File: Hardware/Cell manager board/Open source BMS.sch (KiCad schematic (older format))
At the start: 53 parts, among them P1 CONN_01X07, P2 EXT-TMP, P3 CONN_01X09, P4 CONN_01X09, Q1 BSS138, Q2 BSS138, Q3 BSS138, Q4 BSS138, Q5 BSS138, Q6 BSS138, U1 ATA6870N_BMS

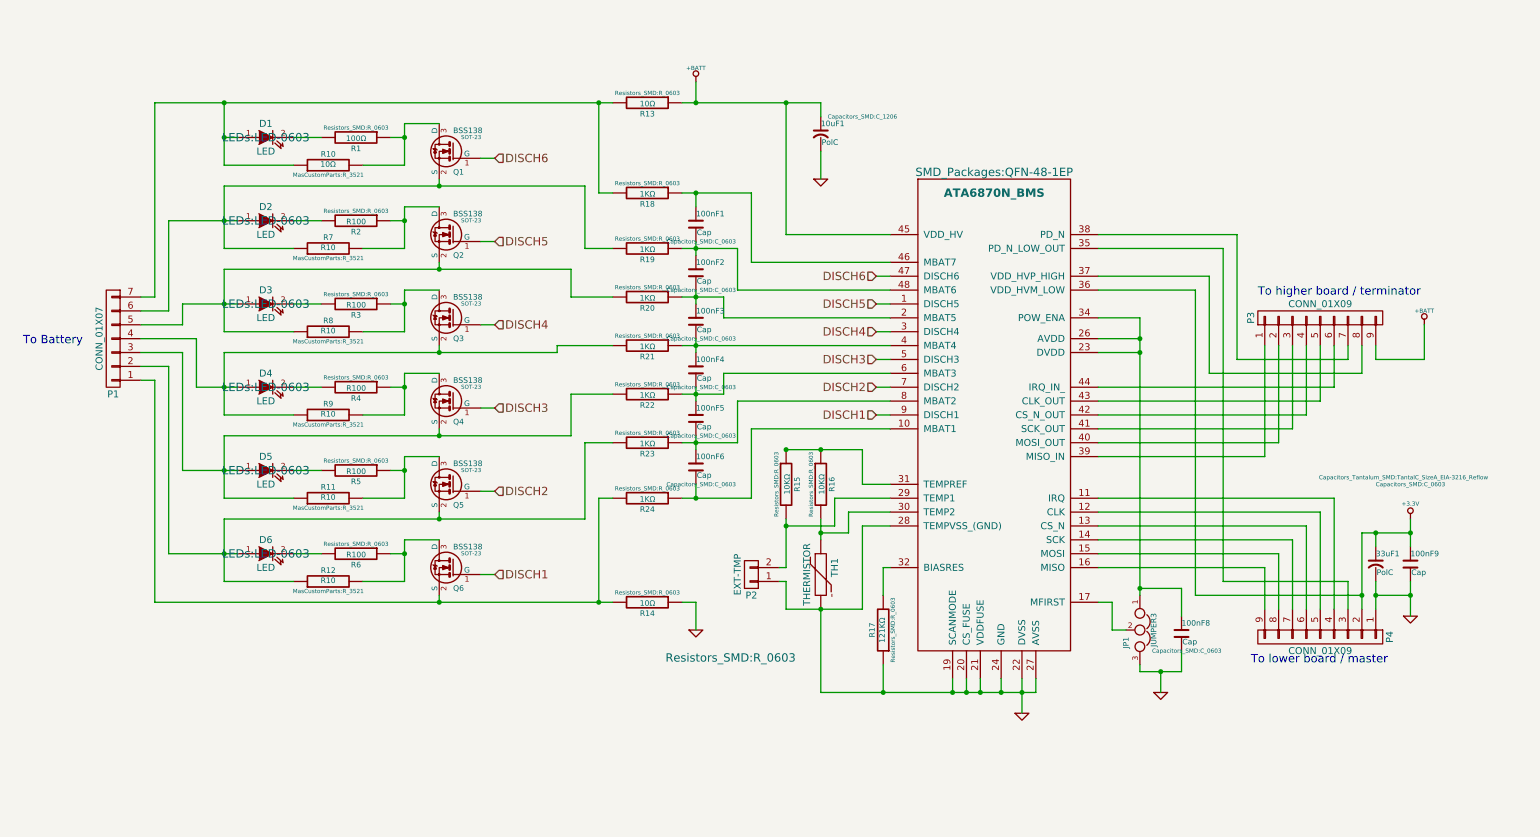
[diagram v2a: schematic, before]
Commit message: cleaned up silkscreen and improved readme
Improved the readme file and added MicroMaster board to it. Also cleaned
up the Slave balance board's silkscreen
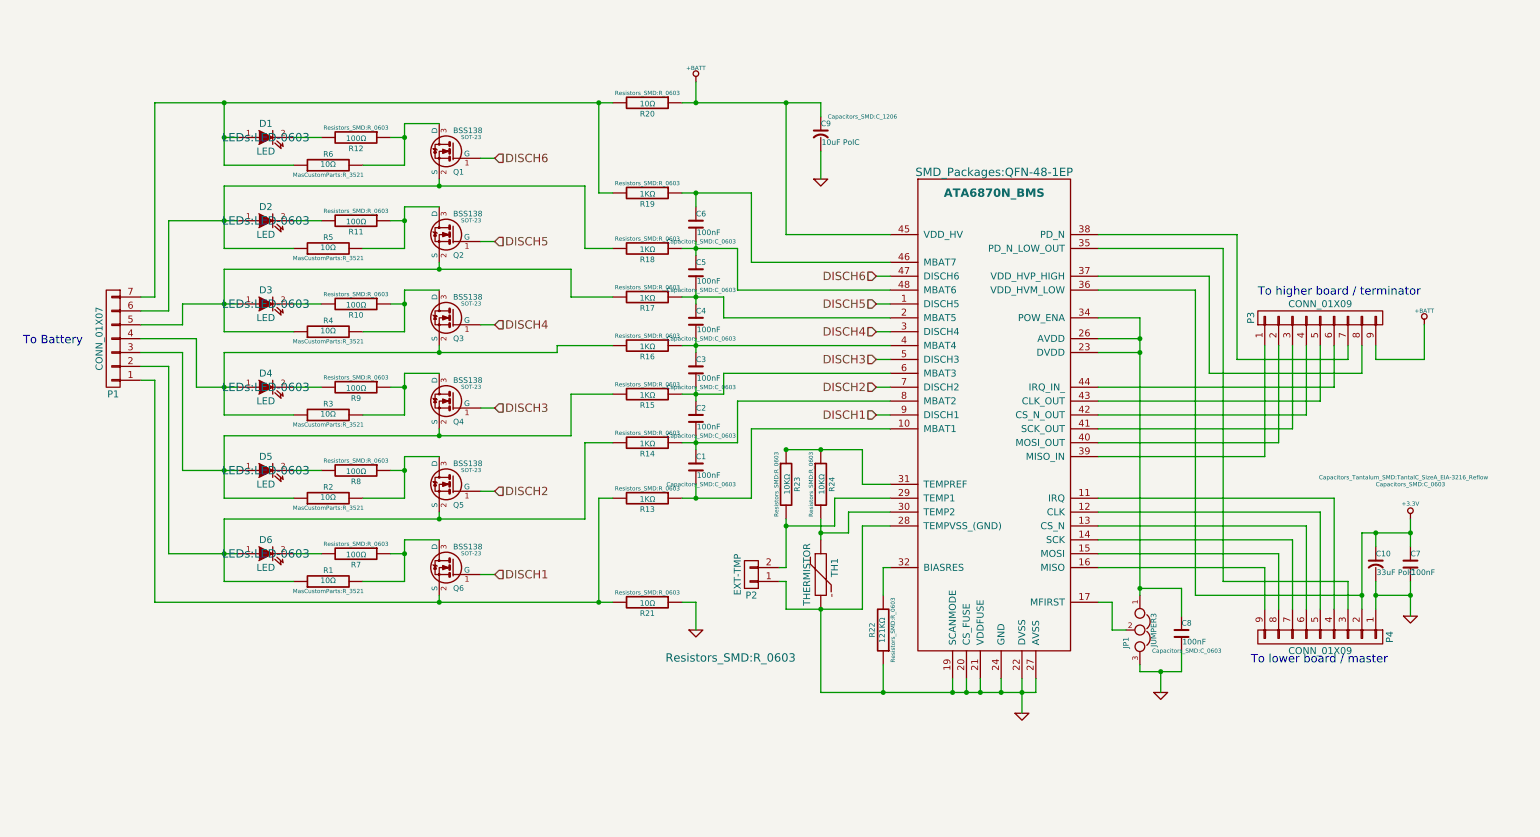
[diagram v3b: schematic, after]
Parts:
- C1: renamed from 100nF6; value Cap -> 100nF
- C10: renamed from 33uF1; value PolC -> 33uF PolC
- C2: renamed from 100nF5; value Cap -> 100nF
- C3: renamed from 100nF4; value Cap -> 100nF
- C4: renamed from 100nF3; value Cap -> 100nF
- C5: renamed from 100nF2; value Cap -> 100nF
- C6: renamed from 100nF1; value Cap -> 100nF
- C7: renamed from 100nF9; value Cap -> 100nF
- C8: renamed from 100nF8; value Cap -> 100nF
- C9: renamed from 10uF1; value PolC -> 10uF PolC
- R1: renamed from R12; value R10 -> 10Ω
- R10: renamed from R3; value R100 -> 100Ω
- R11: renamed from R2; value R100 -> 100Ω
- R2: renamed from R11; value R10 -> 10Ω
- R3: renamed from R9; value R10 -> 10Ω
- R4: renamed from R8; value R10 -> 10Ω
- R5: renamed from R7; value R10 -> 10Ω
- R7: renamed from R6; value R100 -> 100Ω
- R8: renamed from R5; value R100 -> 100Ω
- R9: renamed from R4; value R100 -> 100Ω
- renumbered R1 to R12, R24 to R13, R23 to R14, R22 to R15, R21 to R16, R20 to R17, R19 to R18, R18 to R19, R13 to R20, R14 to R21, R17 to R22, R15 to R23, R16 to R24, R10 to R6
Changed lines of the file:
@@
 $EndComp
 $Comp
-L R R10
+L R R6
 U 1 1 54154E54
 P 2750 1700
-F 0 "R10" V 2830 1700 40  0000 C CNN
+F 0 "R6" V 2830 1700 40  0000 C CNN
 F 1 "10Ω" V 2757 1701 40  0000 C CNN
 F 2 "MasCustomParts:R_3521" V 2680 1700 30  0000 C CNN
@@
 $EndComp
 $Comp
-L R R1
+L R R12
 U 1 1 541899DD
 P 2950 1500
-F 0 "R1" V 3030 1500 40  0000 C CNN
+F 0 "R12" V 3030 1500 40  0000 C CNN
 F 1 "100Ω" V 2957 1501 40  0000 C CNN
 F 2 "Resistors_SMD:R_0603" V 2880 1500 30  0000 C CNN
@@
 $EndComp
 $Comp
-L R R7
+L R R5
 U 1 1 542382CA
 P 2750 2300
-F 0 "R7" V 2830 2300 40  0000 C CNN
-F 1 "R10" V 2757 2301 40  0000 C CNN
+F 0 "R5" V 2830 2300 40  0000 C CNN
+F 1 "10Ω" V 2757 2301 40  0000 C CNN
 F 2 "MasCustomParts:R_3521" V 2680 2300 30  0000 C CNN
 F 3 "" H 2750 2300 30  0000 C CNN
@@
 $EndComp
 $Comp
-L R R2
+L R R11
 U 1 1 542382D0
 P 2950 2100
-F 0 "R2" V 3030 2100 40  0000 C CNN
-F 1 "R100" V 2957 2101 40  0000 C CNN
+F 0 "R11" V 3030 2100 40  0000 C CNN
+F 1 "100Ω" V 2957 2101 40  0000 C CNN
 F 2 "Resistors_SMD:R_0603" V 2880 2100 30  0000 C CNN
 F 3 "" H 2950 2100 30  0000 C CNN
@@
 $EndComp
 $Comp
-L R R8
+L R R4
 U 1 1 5423878A
 P 2750 2900
-F 0 "R8" V 2830 2900 40  0000 C CNN
-F 1 "R10" V 2757 2901 40  0000 C CNN
+F 0 "R4" V 2830 2900 40  0000 C CNN
+F 1 "10Ω" V 2757 2901 40  0000 C CNN
 F 2 "MasCustomParts:R_3521" V 2680 2900 30  0000 C CNN
 F 3 "" H 2750 2900 30  0000 C CNN
@@
 $EndComp
 $Comp
-L R R3
+L R R10
 U 1 1 54238790
 P 2950 2700
-F 0 "R3" V 3030 2700 40  0000 C CNN
-F 1 "R100" V 2957 2701 40  0000 C CNN
+F 0 "R10" V 3030 2700 40  0000 C CNN
+F 1 "100Ω" V 2957 2701 40  0000 C CNN
 F 2 "Resistors_SMD:R_0603" V 2880 2700 30  0000 C CNN
 F 3 "" H 2950 2700 30  0000 C CNN
@@
 $EndComp
 $Comp
-L R R12
+L R R1
 U 1 1 54238D83
 P 2750 4700
-F 0 "R12" V 2830 4700 40  0000 C CNN
-F 1 "R10" V 2757 4701 40  0000 C CNN
+F 0 "R1" V 2830 4700 40  0000 C CNN
+F 1 "10Ω" V 2757 4701 40  0000 C CNN
 F 2 "MasCustomParts:R_3521" V 2680 4700 30  0000 C CNN
 F 3 "" H 2750 4700 30  0000 C CNN
@@
 $EndComp
 $Comp
-L R R6
+L R R7
 U 1 1 54238D89
 P 2950 4500
-F 0 "R6" V 3030 4500 40  0000 C CNN
-F 1 "R100" V 2957 4501 40  0000 C CNN
+F 0 "R7" V 3030 4500 40  0000 C CNN
+F 1 "100Ω" V 2957 4501 40  0000 C CNN
 F 2 "Resistors_SMD:R_0603" V 2880 4500 30  0000 C CNN
 F 3 "" H 2950 4500 30  0000 C CNN
@@
 $EndComp
 $Comp
-L R R9
+L R R3
 U 1 1 54239053
 P 2750 3500
-F 0 "R9" V 2830 3500 40  0000 C CNN
-F 1 "R10" V 2757 3501 40  0000 C CNN
+F 0 "R3" V 2830 3500 40  0000 C CNN
+F 1 "10Ω" V 2757 3501 40  0000 C CNN
 F 2 "MasCustomParts:R_3521" V 2680 3500 30  0000 C CNN
 F 3 "" H 2750 3500 30  0000 C CNN
@@
 $EndComp
 $Comp
-L R R4
+L R R9
 U 1 1 54239059
 P 2950 3300
-F 0 "R4" V 3030 3300 40  0000 C CNN
-F 1 "R100" V 2957 3301 40  0000 C CNN
+F 0 "R9" V 3030 3300 40  0000 C CNN
+F 1 "100Ω" V 2957 3301 40  0000 C CNN
 F 2 "Resistors_SMD:R_0603" V 2880 3300 30  0000 C CNN
 F 3 "" H 2950 3300 30  0000 C CNN
@@
 $EndComp
 $Comp
-L R R11
+L R R2
 U 1 1 542395DF
 P 2750 4100
-F 0 "R11" V 2830 4100 40  0000 C CNN
-F 1 "R10" V 2757 4101 40  0000 C CNN
+F 0 "R2" V 2830 4100 40  0000 C CNN
+F 1 "10Ω" V 2757 4101 40  0000 C CNN
 F 2 "MasCustomParts:R_3521" V 2680 4100 30  0000 C CNN
 F 3 "" H 2750 4100 30  0000 C CNN
@@
 $EndComp
 $Comp
-L R R5
+L R R8
 U 1 1 542395E5
 P 2950 3900
-F 0 "R5" V 3030 3900 40  0000 C CNN
-F 1 "R100" V 2957 3901 40  0000 C CNN
+F 0 "R8" V 3030 3900 40  0000 C CNN
+F 1 "100Ω" V 2957 3901 40  0000 C CNN
 F 2 "Resistors_SMD:R_0603" V 2880 3900 30  0000 C CNN
 F 3 "" H 2950 3900 30  0000 C CNN
@@
 $EndComp
 $Comp
-L R R13
+L R R20
 U 1 1 54244F8C
 P 5050 1250
-F 0 "R13" V 5130 1250 40  0000 C CNN
+F 0 "R20" V 5130 1250 40  0000 C CNN
 F 1 "10Ω" V 5057 1251 40  0000 C CNN
 F 2 "Resistors_SMD:R_0603" V 4980 1250 30  0000 C CNN
@@
 $EndComp
 $Comp
-L R R17
+L R R22
 U 1 1 5424DD8C
 P 6750 5050
-F 0 "R17" V 6830 5050 40  0000 C CNN
+F 0 "R22" V 6830 5050 40  0000 C CNN
 F 1 "121KΩ" V 6757 5051 40  0000 C CNN
 F 2 "Resistors_SMD:R_0603" V 6680 5050 30  0000 C CNN
@@
 $EndComp
 $Comp
-L Cap 100nF2
+L Cap C5
 U 1 1 54250229
 P 5400 2500
-F 0 "100nF2" H 5400 2600 40  0000 L CNN
-F 1 "Cap" H 5406 2465 40  0000 L CNN
+F 0 "C5" H 5400 2600 40  0000 L CNN
+F 1 "100nF" H 5406 2465 40  0000 L CNN
 F 2 "Capacitors_SMD:C_0603" H 5438 2400 30  0000 C CNN
 F 3 "" H 5250 2500 60  0000 C CNN
@@
 $EndComp
 $Comp
-L Cap 100nF4
+L Cap C3
 U 1 1 5425373F
 P 5400 3200
-F 0 "100nF4" H 5400 3300 40  0000 L CNN
-F 1 "Cap" H 5406 3165 40  0000 L CNN
+F 0 "C3" H 5400 3300 40  0000 L CNN
+F 1 "100nF" H 5406 3165 40  0000 L CNN
 F 2 "Capacitors_SMD:C_0603" H 5438 3100 30  0000 C CNN
 F 3 "" H 5250 3200 60  0000 C CNN
@@
 $EndComp
 $Comp
-L Cap 100nF5
+L Cap C2
 U 1 1 54253CD6
 P 5400 3550
-F 0 "100nF5" H 5400 3650 40  0000 L CNN
-F 1 "Cap" H 5406 3515 40  0000 L CNN
+F 0 "C2" H 5400 3650 40  0000 L CNN
+F 1 "100nF" H 5406 3515 40  0000 L CNN
 F 2 "Capacitors_SMD:C_0603" H 5438 3450 30  0000 C CNN
 F 3 "" H 5250 3550 60  0000 C CNN
@@
 $EndComp
 $Comp
-L Cap 100nF6
+L Cap C1
 U 1 1 54253FA8
 P 5400 3900
-F 0 "100nF6" H 5400 4000 40  0000 L CNN
-F 1 "Cap" H 5406 3865 40  0000 L CNN
+F 0 "C1" H 5400 4000 40  0000 L CNN
+F 1 "100nF" H 5406 3865 40  0000 L CNN
 F 2 "Capacitors_SMD:C_0603" H 5438 3800 30  0000 C CNN
 F 3 "" H 5250 3900 60  0000 C CNN
@@
 $EndComp
 $Comp
-L Cap 100nF3
+L Cap C4
 U 1 1 5425B775
 P 5400 2850
-F 0 "100nF3" H 5400 2950 40  0000 L CNN
-F 1 "Cap" H 5406 2815 40  0000 L CNN
+F 0 "C4" H 5400 2950 40  0000 L CNN
+F 1 "100nF" H 5406 2815 40  0000 L CNN
 F 2 "Capacitors_SMD:C_0603" H 5438 2750 30  0000 C CNN
 F 3 "" H 5250 2850 60  0000 C CNN
@@
 $EndComp
 $Comp
-L R R15
+L R R23
 U 1 1 542607A6
 P 6050 4000
-F 0 "R15" V 6130 4000 40  0000 C CNN
+F 0 "R23" V 6130 4000 40  0000 C CNN
 F 1 "10KΩ" V 6057 4001 40  0000 C CNN
 F 2 "Resistors_SMD:R_0603" V 5980 4000 30  0000 C CNN
@@
 $EndComp
 $Comp
-L R R16
+L R R24
 U 1 1 5426080C
 P 6300 4000
-F 0 "R16" V 6380 4000 40  0000 C CNN
+F 0 "R24" V 6380 4000 40  0000 C CNN
 F 1 "10KΩ" V 6307 4001 40  0000 C CNN
 F 2 "Resistors_SMD:R_0603" V 6230 4000 30  0000 C CNN
@@
 $EndComp
 $Comp
-L PolC 33uF1
+L PolC C10
 U 1 1 5426A451
 P 10300 4600
-F 0 "33uF1" H 10300 4700 40  0000 L CNN
-F 1 "PolC" H 10306 4565 40  0000 L CNN
+F 0 "C10" H 10300 4700 40  0000 L CNN
+F 1 "33uF PolC" H 10306 4565 40  0000 L CNN
 F 2 "Capacitors_Tantalum_SMD:TantalC_SizeA_EIA-3216_Reflow" H 10500 5250 30  0000 C CNN
 F 3 "" H 10150 4600 60  0000 C CNN
@@
 $EndComp
 $Comp
-L Cap 100nF9
+L Cap C7
 U 1 1 5425B34F
 P 10550 4600
-F 0 "100nF9" H 10550 4700 40  0000 L CNN
-F 1 "Cap" H 10556 4565 40  0000 L CNN
+F 0 "C7" H 10550 4700 40  0000 L CNN
+F 1 "100nF" H 10556 4565 40  0000 L CNN
 F 2 "Capacitors_SMD:C_0603" H 10550 5200 30  0000 C CNN
 F 3 "" H 10400 4600 60  0000 C CNN
@@
 $EndComp
 $Comp
-L PolC 10uF1
+L PolC C9
 U 1 1 5425B3F6
 P 6300 1500
-F 0 "10uF1" H 6300 1600 40  0000 L CNN
-F 1 "PolC" H 6306 1465 40  0000 L CNN
+F 0 "C9" H 6300 1600 40  0000 L CNN
+F 1 "10uF PolC" H 6306 1465 40  0000 L CNN
 F 2 "Capacitors_SMD:C_1206" H 6600 1650 30  0000 C CNN
 F 3 "" H 6150 1500 60  0000 C CNN
@@
 $EndComp
 $Comp
-L Cap 100nF8
+L Cap C8
 U 1 1 5425D822
 P 8900 5100
-F 0 "100nF8" H 8900 5200 40  0000 L CNN
-F 1 "Cap" H 8906 5065 40  0000 L CNN
+F 0 "C8" H 8900 5200 40  0000 L CNN
+F 1 "100nF" H 8906 5065 40  0000 L CNN
 F 2 "Capacitors_SMD:C_0603" H 8938 5000 30  0000 C CNN
 F 3 "" H 8750 5100 60  0000 C CNN
@@
 Connection ~ 6300 4900
 $Comp
-L R R14
+L R R21
 U 1 1 5426CD58
 P 5050 4850
-F 0 "R14" V 5130 4850 40  0000 C CNN
+F 0 "R21" V 5130 4850 40  0000 C CNN
 F 1 "10Ω" V 5057 4851 40  0000 C CNN
 F 2 "Resistors_SMD:R_0603" V 4980 4850 30  0000 C CNN
@@
 	6700 3100 6800 3100
 $Comp
-L Cap 100nF1
+L Cap C6
 U 1 1 5425017E
 P 5400 2150
-F 0 "100nF1" H 5400 2250 40  0000 L CNN
-F 1 "Cap" H 5406 2115 40  0000 L CNN
+F 0 "C6" H 5400 2250 40  0000 L CNN
+F 1 "100nF" H 5406 2115 40  0000 L CNN
 F 2 "Capacitors_SMD:C_0603" H 5438 2050 30  0000 C CNN
 F 3 "" H 5250 2150 60  0000 C CNN
@@
 Connection ~ 5400 3700
 $Comp
-L R R21
+L R R16
 U 1 1 5426CCBC
 P 5050 3000
-F 0 "R21" V 5130 3000 40  0000 C CNN
+F 0 "R16" V 5130 3000 40  0000 C CNN
 F 1 "1KΩ" V 5057 3001 40  0000 C CNN
 F 2 "Resistors_SMD:R_0603" V 4980 3000 30  0000 C CNN
@@
 $EndComp
 $Comp
-L R R22
+L R R15
 U 1 1 5426CD15
 P 5050 3350
-F 0 "R22" V 5130 3350 40  0000 C CNN
+F 0 "R15" V 5130 3350 40  0000 C CNN
 F 1 "1KΩ" V 5057 3351 40  0000 C CNN
 F 2 "Resistors_SMD:R_0603" V 4980 3350 30  0000 C CNN
@@
 $EndComp
 $Comp
-L R R23
+L R R14
 U 1 1 5426CD61
 P 5050 3700
-F 0 "R23" V 5130 3700 40  0000 C CNN
+F 0 "R14" V 5130 3700 40  0000 C CNN
 F 1 "1KΩ" V 5057 3701 40  0000 C CNN
 F 2 "Resistors_SMD:R_0603" V 4980 3700 30  0000 C CNN
@@
 $EndComp
 $Comp
-L R R24
+L R R13
 U 1 1 5426CFD2
 P 5050 4100
-F 0 "R24" V 5130 4100 40  0000 C CNN
+F 0 "R13" V 5130 4100 40  0000 C CNN
 F 1 "1KΩ" V 5057 4101 40  0000 C CNN
 F 2 "Resistors_SMD:R_0603" V 4980 4100 30  0000 C CNN
@@
 	4500 2650 4500 2450
 $Comp
-L R R20
+L R R17
 U 1 1 5427A4E8
 P 5050 2650
-F 0 "R20" V 5130 2650 40  0000 C CNN
+F 0 "R17" V 5130 2650 40  0000 C CNN
 F 1 "1KΩ" V 5057 2651 40  0000 C CNN
 F 2 "Resistors_SMD:R_0603" V 4980 2650 30  0000 C CNN
@@
 $EndComp
 $Comp
-L R R19
+L R R18
 U 1 1 5427A5D8
 P 5050 2300
-F 0 "R19" V 5130 2300 40  0000 C CNN
+F 0 "R18" V 5130 2300 40  0000 C CNN
 F 1 "1KΩ" V 5057 2301 40  0000 C CNN
 F 2 "Resistors_SMD:R_0603" V 4980 2300 30  0000 C CNN
@@
 $EndComp
 $Comp
-L R R18
+L R R19
 U 1 1 5427A691
 P 5050 1900
-F 0 "R18" V 5130 1900 40  0000 C CNN
+F 0 "R19" V 5130 1900 40  0000 C CNN
 F 1 "1KΩ" V 5057 1901 40  0000 C CNN
 F 2 "Resistors_SMD:R_0603" V 4980 1900 30  0000 C CNN

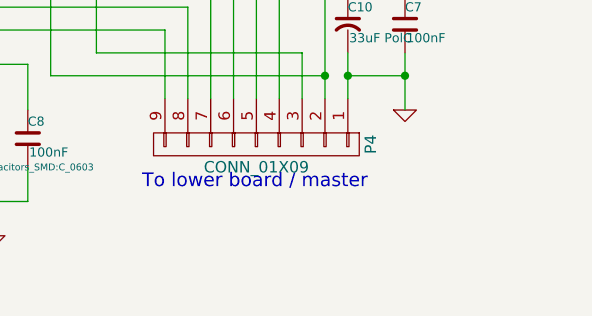
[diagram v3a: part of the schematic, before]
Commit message: finished resistor change and via stiching
finished resistor change and via stiching. board is now functional (at
least I hope) the last thing to do is tidy up the silkscreen and
soldermask
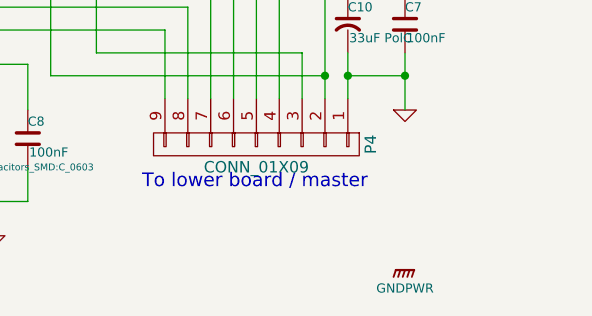
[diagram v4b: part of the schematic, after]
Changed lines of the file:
@@
 Text Notes 9450 2650 0    60   ~ 0
 To higher board / terminator
+$Comp
+L GNDPWR #PWR?
+U 1 1 543C5063
+P 10550 5650
+F 0 "#PWR?" H 10550 5700 40  0001 C CNN
+F 1 "GNDPWR" H 10550 5570 40  0000 C CNN
+F 2 "" H 10550 5650 60  0000 C CNN
+F 3 "" H 10550 5650 60  0000 C CNN
+	1    10550 5650
+	1    0    0    -1
+$EndComp
 $EndSCHEMATC
